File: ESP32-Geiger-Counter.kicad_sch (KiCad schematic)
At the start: 70 parts, among them J1 2s1p Lipo Battery Pack (8.4V-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, J2 USB_C_Receptacle_USB2.0_16P, J3 SBM20 +, J4 SBM20 -, Q1 Q_NMOS_GDS, Q2 2N3904, SW1 SW_SPDT, SW2 RESET, SW3 BOOT, U1 BQ25886RGE, U2 AP63203WU, U3 ESP32-S3-WROOM-1, U4 UCC27517DBVR

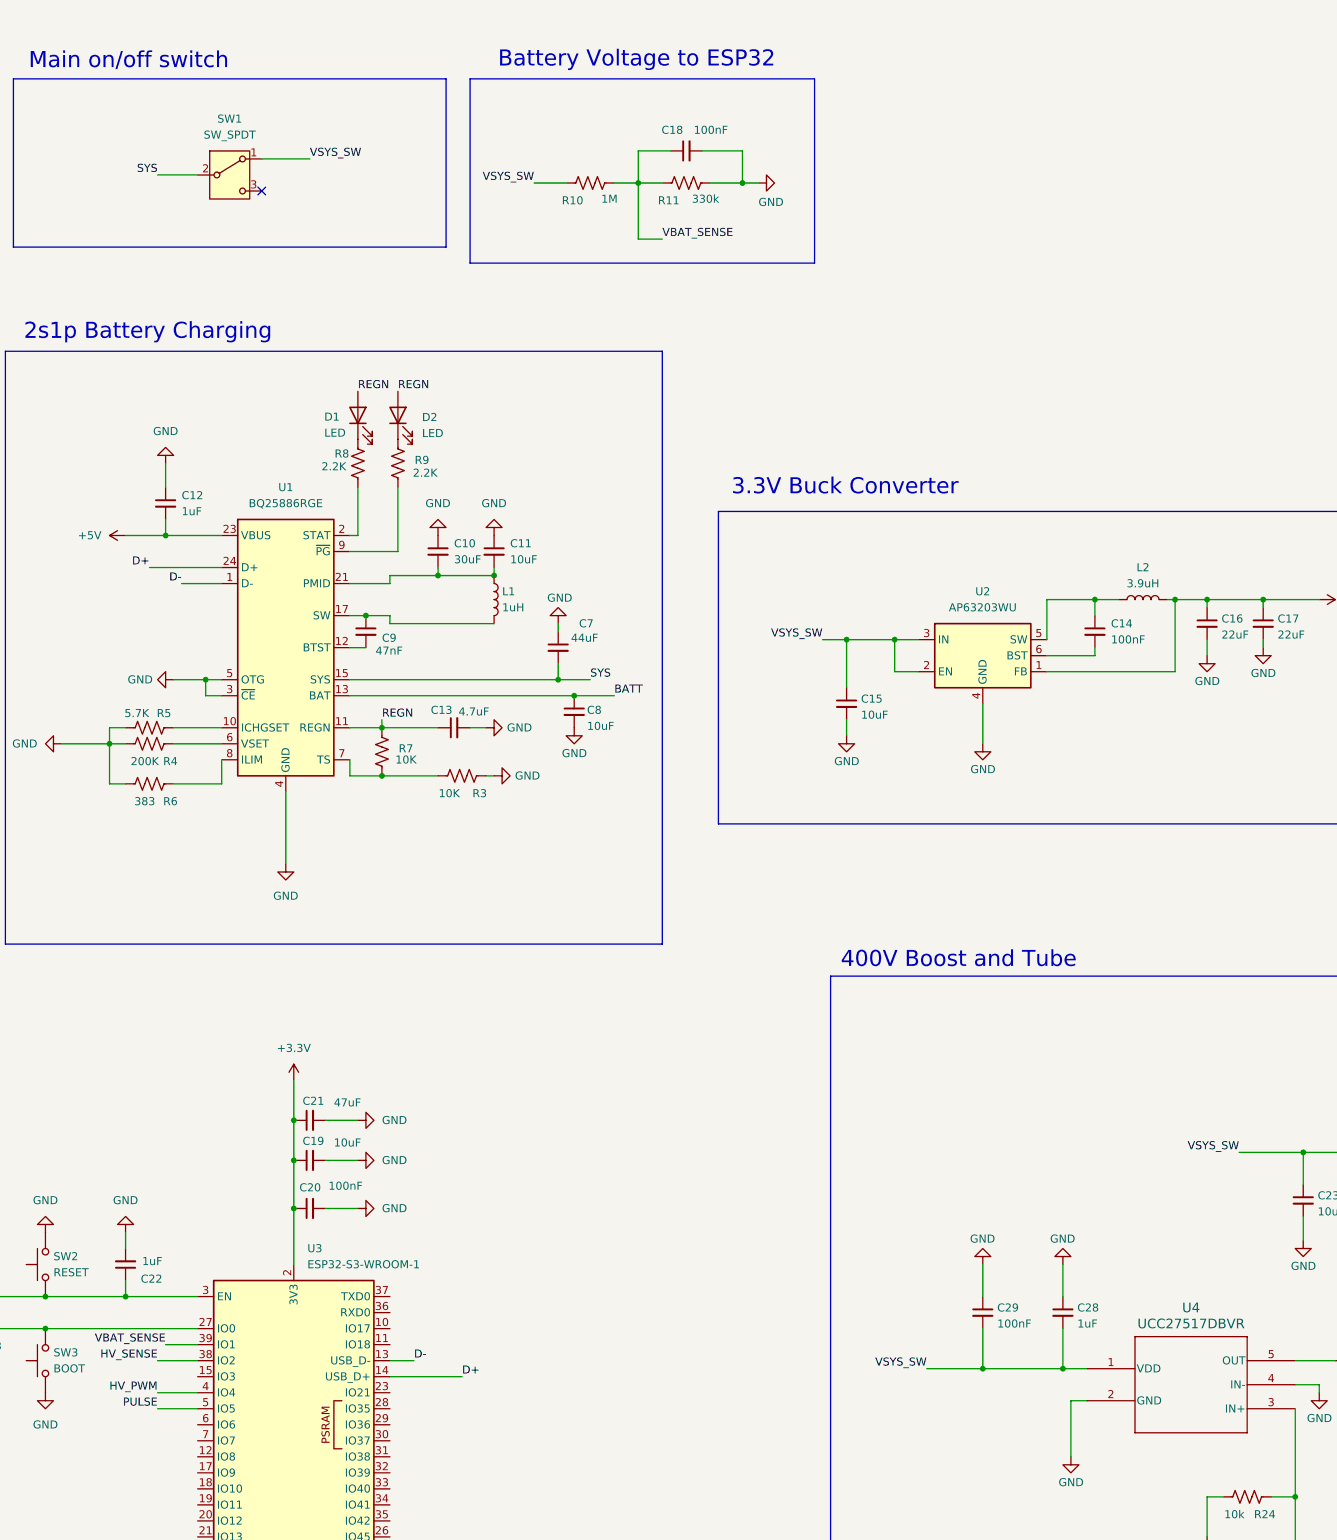
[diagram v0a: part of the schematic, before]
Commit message: added piezo speaker
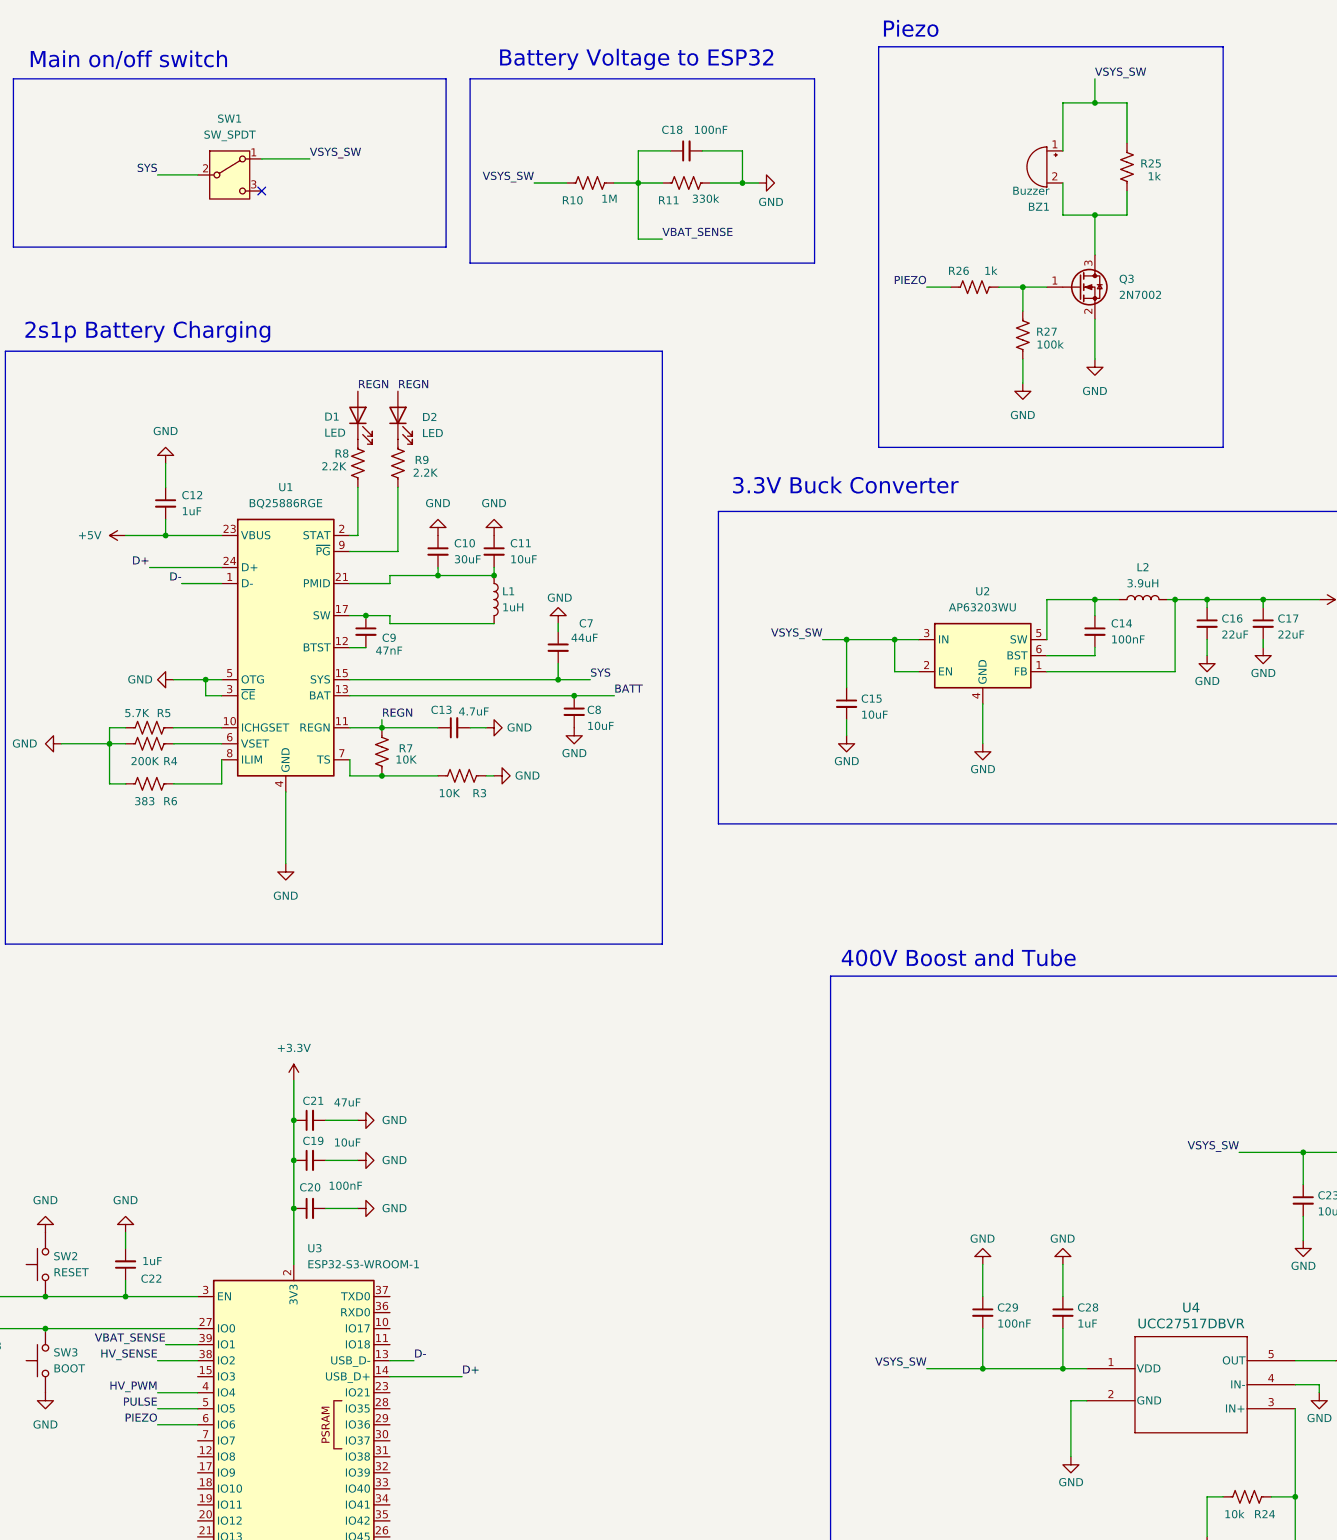
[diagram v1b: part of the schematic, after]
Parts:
- added BZ1: Buzzer, symbol Device:Buzzer
- added Q3: 2N7002, Package_TO_SOT_SMD:SOT-23, symbol Transistor_FET:2N7002
- added R25, R26: 1k, symbol Device:R_US
- added R27: 100k, symbol Device:R_US
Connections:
- net GND: now also Q3.2 (S), R27.1
- net VSYS_SW: now also BZ1.1 (+), R25.2
- net PIEZO: now reaches U3.6 (IO6)
- net PIEZO: now also R26.2
- new net: BZ1.2 (-), Q3.3 (D), R25.1
- new net: Q3.1 (G), R26.1, R27.2
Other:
- note added: "Piezo"

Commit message: added SSD1309 oled screen
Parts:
- added C30: 10uF, symbol Device:C_Small
- added C31: 100nF, symbol Device:C_Small
- added J5: Conn_01x07, symbol Connector_Generic:Conn_01x07
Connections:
- net +3.3V: now also C30.2, C31.2, J5.2 (Pin_2)
- net GND: now also C30.1, C31.1, J5.1 (Pin_1)
- net OLED_CS: now reaches U3.18 (IO10)
- net OLED_CS: now also J5.7 (Pin_7)
- net OLED_MOSI: now reaches U3.19 (IO11)
- net OLED_MOSI: now also J5.4 (Pin_4)
- net OLED_SCK: now reaches U3.20 (IO12)
- net OLED_SCK: now also J5.3 (Pin_3)
- net OLED_DC: now reaches U3.21 (IO13)
- net OLED_DC: now also J5.6 (Pin_6)
- net OLED_RST: now reaches U3.23 (IO21)
- net OLED_RST: now also J5.5 (Pin_5)
- no-connect marks 3 -> 26
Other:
- note added: "SSD1309 OLED Screen"

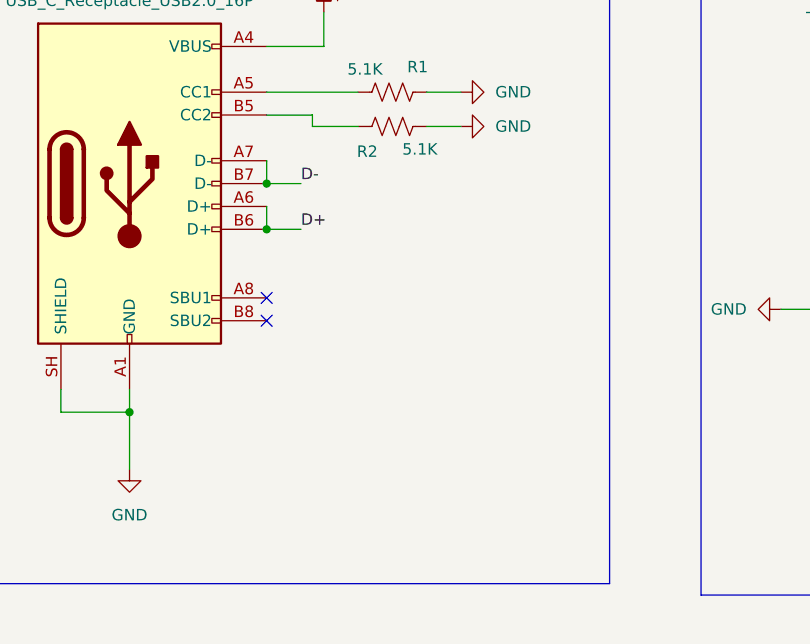
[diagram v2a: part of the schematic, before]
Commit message: added tvs diode protection for usb c
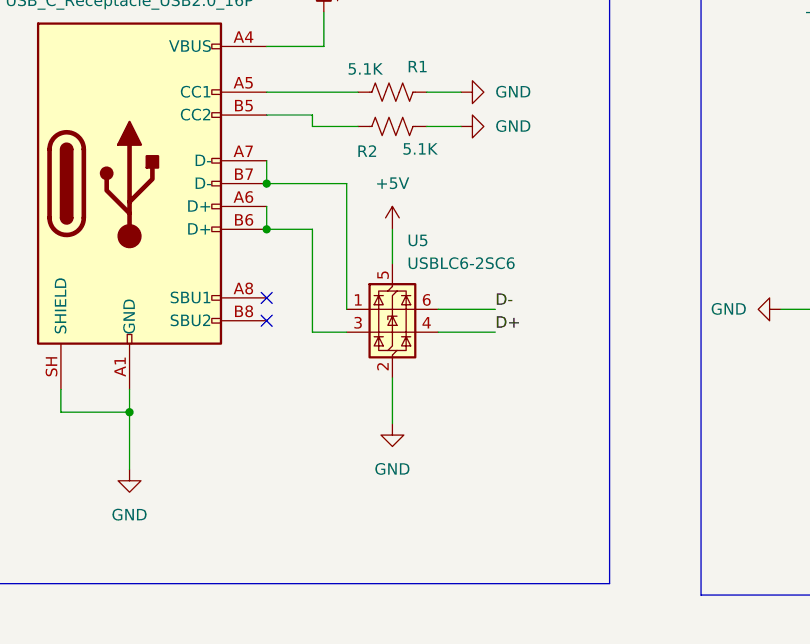
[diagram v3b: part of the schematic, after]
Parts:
- added U5: USBLC6-2SC6, Package_TO_SOT_SMD:SOT-23-6, symbol Power_Protection:USBLC6-2SC6
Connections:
- net +5V: now also U5.5 (VBUS)
- net D+: now also U5.4 (I/O2); no longer J2.A6 (D+), J2.B6 (D+)
- net D-: now also U5.6 (I/O1); no longer J2.A7 (D-), J2.B7 (D-)
- net GND: now also U5.2 (GND)
- new net: J2.A6 (D+), J2.B6 (D+), U5.3 (I/O2)
- new net: J2.A7 (D-), J2.B7 (D-), U5.1 (I/O1)

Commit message: small tweaks
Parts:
- C10: value 30uF -> 22uF
- D3: value 1000V -> US1M
- R5: value 5.7K -> 5.76K
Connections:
- net BATT: now also R10.2
- net VSYS_SW: no longer R10.2
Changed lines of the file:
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@@
 		)
 	)
-	(label "VSYS_SW"
+	(label "BATT"
 		(at 201.93 45.72 180)
 		(effects
@@
 			)
 		)
-		(property "Value" "1000V"
+		(property "Value" "US1M"
 			(at 359.41 195.58 0)
 			(show_name no)
@@
 			)
 		)
-		(property "Value" "5.7K"
+		(property "Value" "5.76K"
 			(at 138.938 129.794 90)
 			(show_name no)
@@
 			)
 		)
-		(property "Value" "30uF"
+		(property "Value" "22uF"
 			(at 189.23 105.4162 0)
 			(show_name no)

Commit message: added a bunch of passive footprints
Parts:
- C14, C17, C18, C26, C28, C29, C31: footprint (none) -> Capacitor_SMD:C_0805_2012Metric
- C15, C16, C23, C24, C25, C27, C30: footprint (none) -> Capacitor_SMD:C_1206_3216Metric
- D3, D4, D5, D6: footprint (none) -> Diode_SMD:D_SMA
- F1: footprint (none) -> Fuse:Fuse_2920_7451Metric
- R1, R10, R11, R17, R2, R20, R21, R22, R23, R24, R25, R26, R27: footprint (none) -> Resistor_SMD:R_0805_2012Metric
- R14, R15, R16: footprint (none) -> Resistor_SMD:R_1206_3216Metric
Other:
- note added: "ESP32"
- moved on the sheet: C19, C20, C21, C22, R12, R13, SW2, SW3, U3

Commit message: added more passive footprints
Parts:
- C10, C11: footprint (none) -> Capacitor_SMD:C_1206_3216Metric
- C12, C13, C9: footprint (none) -> Capacitor_SMD:C_0805_2012Metric
- D1, D2: footprint (none) -> LED_SMD:LED_0805_2012Metric
- R3, R4, R5, R6, R7, R8, R9: footprint (none) -> Resistor_SMD:R_0805_2012Metric
- SW1: footprint (none) -> Button_Switch_THT:SW_Slide_SPDT_Straight_CK_OS102011MS2Q
- SW2, SW3: footprint (none) -> Button_Switch_SMD:SW_SPST_TL3342
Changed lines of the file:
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@@
 			)
 		)
-		(property "Footprint" ""
+		(property "Footprint" "Resistor_SMD:R_0805_2012Metric"
 			(at 179.324 89.916 90)
 			(hide yes)
@@
 			)
 		)
-		(property "Footprint" ""
+		(property "Footprint" "LED_SMD:LED_0805_2012Metric"
 			(at 180.34 82.55 0)
 			(hide yes)
@@
 			)
 		)
-		(property "Footprint" ""
+		(property "Footprint" "Capacitor_SMD:C_0805_2012Metric"
 			(at 189.23 132.08 0)
 			(hide yes)
@@
 			)
 		)
-		(property "Footprint" ""
+		(property "Footprint" "Resistor_SMD:R_0805_2012Metric"
 			(at 140.716 133.096 90)
 			(hide yes)
@@
 			)
 		)
-		(property "Footprint" ""
+		(property "Footprint" "Resistor_SMD:R_0805_2012Metric"
 			(at 141.224 139.954 90)
 			(hide yes)
@@
 			)
 		)
-		(property "Footprint" ""
+		(property "Footprint" "LED_SMD:LED_0805_2012Metric"
 			(at 173.99 82.55 0)
 			(hide yes)
@@
 			)
 		)
-		(property "Footprint" ""
+		(property "Footprint" "Resistor_SMD:R_0805_2012Metric"
 			(at 141.224 133.604 90)
 			(hide yes)
@@
 			)
 		)
-		(property "Footprint" ""
+		(property "Footprint" "Button_Switch_SMD:SW_SPST_TL3342"
 			(at 87.63 242.57 0)
 			(hide yes)
@@
 			)
 		)
-		(property "Footprint" ""
+		(property "Footprint" "Button_Switch_SMD:SW_SPST_TL3342"
 			(at 87.63 227.33 0)
 			(hide yes)
@@
 			)
 		)
-		(property "Footprint" ""
+		(property "Footprint" "Capacitor_SMD:C_0805_2012Metric"
 			(at 175.26 116.84 0)
 			(hide yes)
@@
 			)
 		)
-		(property "Footprint" ""
+		(property "Footprint" "Resistor_SMD:R_0805_2012Metric"
 			(at 176.784 135.636 90)
 			(hide yes)
@@
 			)
 		)
-		(property "Footprint" ""
+		(property "Footprint" "Resistor_SMD:R_0805_2012Metric"
 			(at 172.974 89.916 90)
 			(hide yes)
@@
 			)
 		)
-		(property "Footprint" ""
+		(property "Footprint" "Button_Switch_THT:SW_Slide_SPDT_Straight_CK_OS102011MS2Q"
 			(at 153.67 44.45 0)
 			(hide yes)
@@
 			)
 		)
-		(property "Footprint" ""
+		(property "Footprint" "Resistor_SMD:R_0805_2012Metric"
 			(at 190.754 138.684 90)
 			(hide yes)
@@
 			)
 		)
-		(property "Footprint" ""
+		(property "Footprint" "Capacitor_SMD:C_1206_3216Metric"
 			(at 195.58 104.14 0)
 			(hide yes)
@@
 			)
 		)
-		(property "Footprint" ""
+		(property "Footprint" "Capacitor_SMD:C_1206_3216Metric"
 			(at 186.69 104.14 0)
 			(hide yes)
@@
 			)
 		)
-		(property "Footprint" ""
+		(property "Footprint" "Capacitor_SMD:C_0805_2012Metric"
 			(at 143.51 96.52 0)
 			(hide yes)

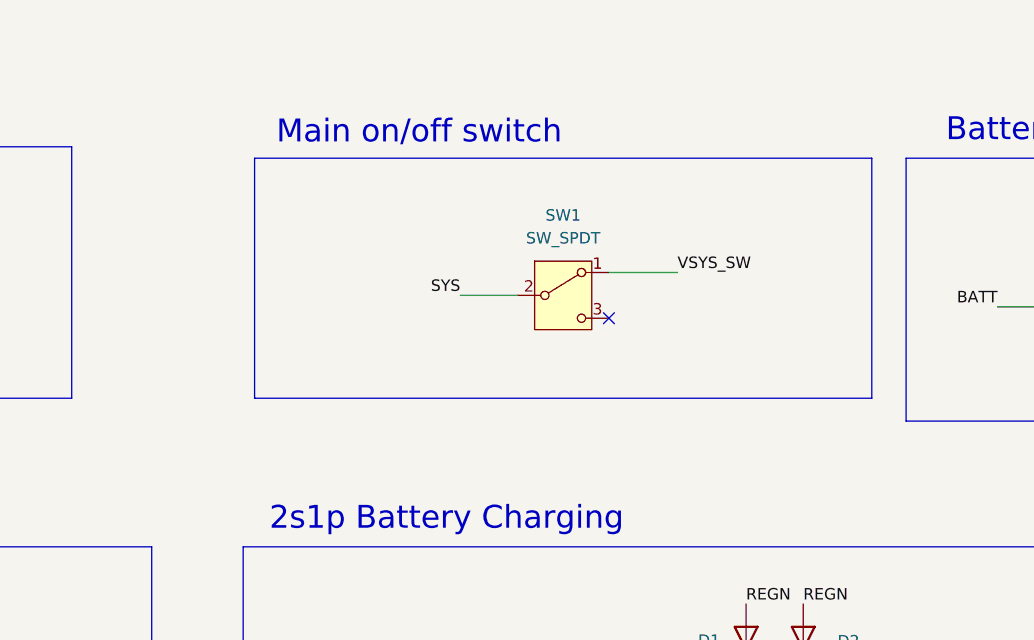
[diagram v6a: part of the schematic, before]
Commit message: made power switch power a fet instead of switching entire current
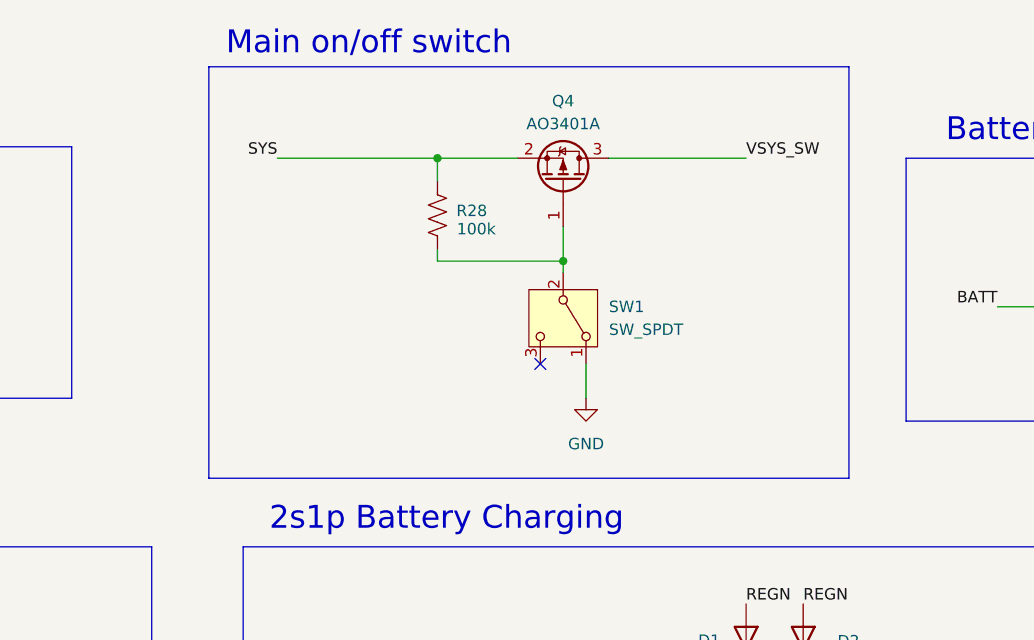
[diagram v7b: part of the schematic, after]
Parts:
- added Q4: AO3401A, Package_TO_SOT_SMD:SOT-23, symbol Transistor_FET:AO3401A
- added R28: 100k, Resistor_SMD:R_0805_2012Metric, symbol Device:R_US
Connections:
- net GND: now also SW1.1 (A)
- net SYS: now also Q4.2 (S), R28.2; no longer SW1.2 (B)
- net VSYS_SW: now also Q4.3 (D); no longer SW1.1 (A)
- new net: Q4.1 (G), R28.1, SW1.2 (B)
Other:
- moved on the sheet: SW1
